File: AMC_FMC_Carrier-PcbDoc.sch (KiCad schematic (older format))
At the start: 17 parts

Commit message: Add two mounting holes
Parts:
- added B11, B12: PLATED_HOLE2.7_PAD5.0, Marble:HOLE2.7_PAD5.0, symbol Pads:PLATED_HOLE2.7_PAD5.0
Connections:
- wire segments 366 -> 368
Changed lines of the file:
@@
 	3400 15500 3600 15500
 Connection ~ 3400 15500
+$Comp
+L Pads:PLATED_HOLE2.7_PAD5.0 B11
+U 1 1 5ECD5570
+P 4000 15250
+F 0 "B11" H 3985 15355 50  0000 C CNN
+F 1 "PLATED_HOLE2.7_PAD5.0" H 4000 15080 60  0001 L CNN
+F 2 "Marble:HOLE2.7_PAD5.0" H 4000 14270 60  0001 L CNN
+F 3 "" H 4000 14900 60  0001 L CNN
+F 4 "Plated Hole" H 4000 14810 60  0001 L CNN "Pole4"
+F 5 "PLATED_HOLE2.7_PAD5.0" H 4000 14810 60  0001 L CNN "Part Number"
+F 6 "Single Terminal Socket" H 4000 14720 60  0001 L CNN "Library Ref"
+F 7 "SchLib\\Pads.SchLib" H 4000 14630 60  0001 L CNN "Library Path"
+F 8 " " H 4000 14540 60  0001 L CNN "Comment"
+F 9 "Standard (No BOM)" H 4000 14450 60  0001 L CNN "Component Kind"
+F 10 "Standard (No BOM)" H 4000 14360 60  0001 L CNN "Component Type"
+F 11 "1" H 4000 14180 60  0001 L CNN "Pin Count"
+F 12 " " H 4000 14090 60  0001 L CNN "Case"
+F 13 "PcbLib\\Pads.PcbLib" H 4000 14000 60  0001 L CNN "Footprint Path"
+F 14 "MTG270_500" H 4000 13910 60  0001 L CNN "Footprint Ref"
+F 15 "Plated Hole" H 4000 13820 60  0001 L CNN "Family"
+F 16 "No" H 4000 13730 60  0001 L CNN "Mounted"
+F 17 "No" H 4000 13640 60  0001 L CNN "Socket"
+F 18 "No" H 4000 13550 60  0001 L CNN "SMD"
+F 19 "No" H 4000 13460 60  0001 L CNN "Sense"
+F 20 " " H 4000 13370 60  0001 L CNN "Sense Comment"
+F 21 "None" H 4000 13280 60  0001 L CNN "Status"
+F 22 " " H 4000 13190 60  0001 L CNN "Status Comment"
+F 23 "Plated Through Hole: Hole Dia.=2.7mm Pad Dia.=5.0mm" H 4000 13010 60  0001 L CNN "Part Description"
+F 24 " " H 4000 12920 60  0001 L CNN "Manufacturer"
+F 25 " " H 4000 12830 60  0001 L CNN "Manufacturer Part Number"
+F 26 "0mm" H 4000 12740 60  0001 L CNN "ComponentHeight"
+F 27 " " H 4000 12650 60  0001 L CNN "Manufacturer1 Example"
+F 28 " " H 4000 12560 60  0001 L CNN "Manufacturer1 Part Number"
+F 29 " " H 4000 12470 60  0001 L CNN "Manufacturer1 ComponentHeight"
+F 30 " " H 4000 12200 60  0001 L CNN "ComponentLink1Description"
+F 31 " " H 4000 12020 60  0001 L CNN "ComponentLink2Description"
+F 32 "CERN DEM JMW" H 4000 11930 60  0001 L CNN "Author"
+F 33 "09/27/11 00:00:00" H 4000 11840 60  0001 L CNN "CreateDate"
+F 34 "09/27/11 00:00:00" H 4000 11750 60  0001 L CNN "LatestRevisionDate"
+F 35 "Plated Through Hole: Hole Dia.=2.7mm Pad Dia.=5.0mm" H 4000 11660 60  0001 L CNN "PackageDescription"
+F 36 "Eletro-mechanical.DbLib" H 4000 11570 60  0001 L CNN "Library Name"
+F 37 "This work is licensed under the Creative Commons CC-BY-SA 4.0 License. To the extent that circuit schematics that use Licensed Material can be considered to be ‘Adapted Material’, then the copyright holder waives article 3.b of the license with respect to these schematics." H 4000 11480 60  0001 L CNN "License"
+F 38 "dnf" H 4000 15250 50  0001 C CNN "config"
+	1    4000 15250
+	1    0    0    -1
+$EndComp
+$Comp
+L Pads:PLATED_HOLE2.7_PAD5.0 B12
+U 1 1 5ECD6329
+P 4150 15250
+F 0 "B12" H 4135 15355 50  0000 C CNN
+F 1 "PLATED_HOLE2.7_PAD5.0" H 4150 15080 60  0001 L CNN
+F 2 "Marble:HOLE2.7_PAD5.0" H 4150 14270 60  0001 L CNN
+F 3 "" H 4150 14900 60  0001 L CNN
+F 4 "Plated Hole" H 4150 14810 60  0001 L CNN "Pole4"
+F 5 "PLATED_HOLE2.7_PAD5.0" H 4150 14810 60  0001 L CNN "Part Number"
+F 6 "Single Terminal Socket" H 4150 14720 60  0001 L CNN "Library Ref"
+F 7 "SchLib\\Pads.SchLib" H 4150 14630 60  0001 L CNN "Library Path"
+F 8 " " H 4150 14540 60  0001 L CNN "Comment"
+F 9 "Standard (No BOM)" H 4150 14450 60  0001 L CNN "Component Kind"
+F 10 "Standard (No BOM)" H 4150 14360 60  0001 L CNN "Component Type"
+F 11 "1" H 4150 14180 60  0001 L CNN "Pin Count"
+F 12 " " H 4150 14090 60  0001 L CNN "Case"
+F 13 "PcbLib\\Pads.PcbLib" H 4150 14000 60  0001 L CNN "Footprint Path"
+F 14 "MTG270_500" H 4150 13910 60  0001 L CNN "Footprint Ref"
+F 15 "Plated Hole" H 4150 13820 60  0001 L CNN "Family"
+F 16 "No" H 4150 13730 60  0001 L CNN "Mounted"
+F 17 "No" H 4150 13640 60  0001 L CNN "Socket"
+F 18 "No" H 4150 13550 60  0001 L CNN "SMD"
+F 19 "No" H 4150 13460 60  0001 L CNN "Sense"
+F 20 " " H 4150 13370 60  0001 L CNN "Sense Comment"
+F 21 "None" H 4150 13280 60  0001 L CNN "Status"
+F 22 " " H 4150 13190 60  0001 L CNN "Status Comment"
+F 23 "Plated Through Hole: Hole Dia.=2.7mm Pad Dia.=5.0mm" H 4150 13010 60  0001 L CNN "Part Description"
+F 24 " " H 4150 12920 60  0001 L CNN "Manufacturer"
+F 25 " " H 4150 12830 60  0001 L CNN "Manufacturer Part Number"
+F 26 "0mm" H 4150 12740 60  0001 L CNN "ComponentHeight"
+F 27 " " H 4150 12650 60  0001 L CNN "Manufacturer1 Example"
+F 28 " " H 4150 12560 60  0001 L CNN "Manufacturer1 Part Number"
+F 29 " " H 4150 12470 60  0001 L CNN "Manufacturer1 ComponentHeight"
+F 30 " " H 4150 12200 60  0001 L CNN "ComponentLink1Description"
+F 31 " " H 4150 12020 60  0001 L CNN "ComponentLink2Description"
+F 32 "CERN DEM JMW" H 4150 11930 60  0001 L CNN "Author"
+F 33 "09/27/11 00:00:00" H 4150 11840 60  0001 L CNN "CreateDate"
+F 34 "09/27/11 00:00:00" H 4150 11750 60  0001 L CNN "LatestRevisionDate"
+F 35 "Plated Through Hole: Hole Dia.=2.7mm Pad Dia.=5.0mm" H 4150 11660 60  0001 L CNN "PackageDescription"
+F 36 "Eletro-mechanical.DbLib" H 4150 11570 60  0001 L CNN "Library Name"
+F 37 "This work is licensed under the Creative Commons CC-BY-SA 4.0 License. To the extent that circuit schematics that use Licensed Material can be considered to be ‘Adapted Material’, then the copyright holder waives article 3.b of the license with respect to these schematics." H 4150 11480 60  0001 L CNN "License"
+F 38 "dnf" H 4150 15250 50  0001 C CNN "config"
+	1    4150 15250
+	1    0    0    -1
+$EndComp
+$Comp
+L power:GND #PWR?
+U 1 1 5ECDA445
+P 4350 15250
+AR Path="/5BD32060/5ECDA445" Ref="#PWR?"  Part="1"
+AR Path="/5BABAC65/5ECDA445" Ref="#PWR?"  Part="1"
+AR Path="/5CC24E97/5ECDA445" Ref="#PWR?"  Part="1"
+AR Path="/5CC393D3/5ECDA445" Ref="#PWR?"  Part="1"
+AR Path="/5CC6DBF7/5ECDA445" Ref="#PWR?"  Part="1"
+AR Path="/5CC8AFE1/5ECDA445" Ref="#PWR?"  Part="1"
+AR Path="/5BCEDA3D/5ECDA445" Ref="#PWR?"  Part="1"
+AR Path="/5ECDA445" Ref="#PWR?"  Part="1"
+F 0 "#PWR?" H 4350 15000 50  0001 C CNN
+F 1 "GND" H 4355 15077 50  0000 C CNN
+F 2 "" H 4350 15250 50  0001 C CNN
+F 3 "" H 4350 15250 50  0001 C CNN
+	1    4350 15250
+	1    0    0    -1
+$EndComp
+Wire Wire Line
+	4000 15250 4150 15250
+Wire Wire Line
+	4150 15250 4350 15250
+Connection ~ 4150 15250
 $EndSCHEMATC

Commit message: More attribute fixes
Fix up Attribute names in HDT0001 and AG5300
Remove stray attribute for SN65MLVD2DRBT (added in last commit)
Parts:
- S1: Manufacturer (none) -> C & K COMPONENTS; Manufacturer_Name C & K COMPONENTS -> (none)
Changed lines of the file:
@@
 F 4 "HDT0001 (Detector Switches)" H 4000 9100 50  0001 L CNN "Description"
 F 5 "3" H 4000 9000 50  0001 L CNN "Height"
-F 6 "C & K COMPONENTS" H 4000 8900 50  0001 L CNN "Manufacturer_Name"
+F 6 "C & K COMPONENTS" H 4000 8900 50  0001 L CNN "Manufacturer"
 F 7 "HDT0001" H 4000 8800 50  0001 L CNN "Manufacturer Part Number"
 F 8 "7931598" H 4000 8700 50  0001 L CNN "RS Part Number"

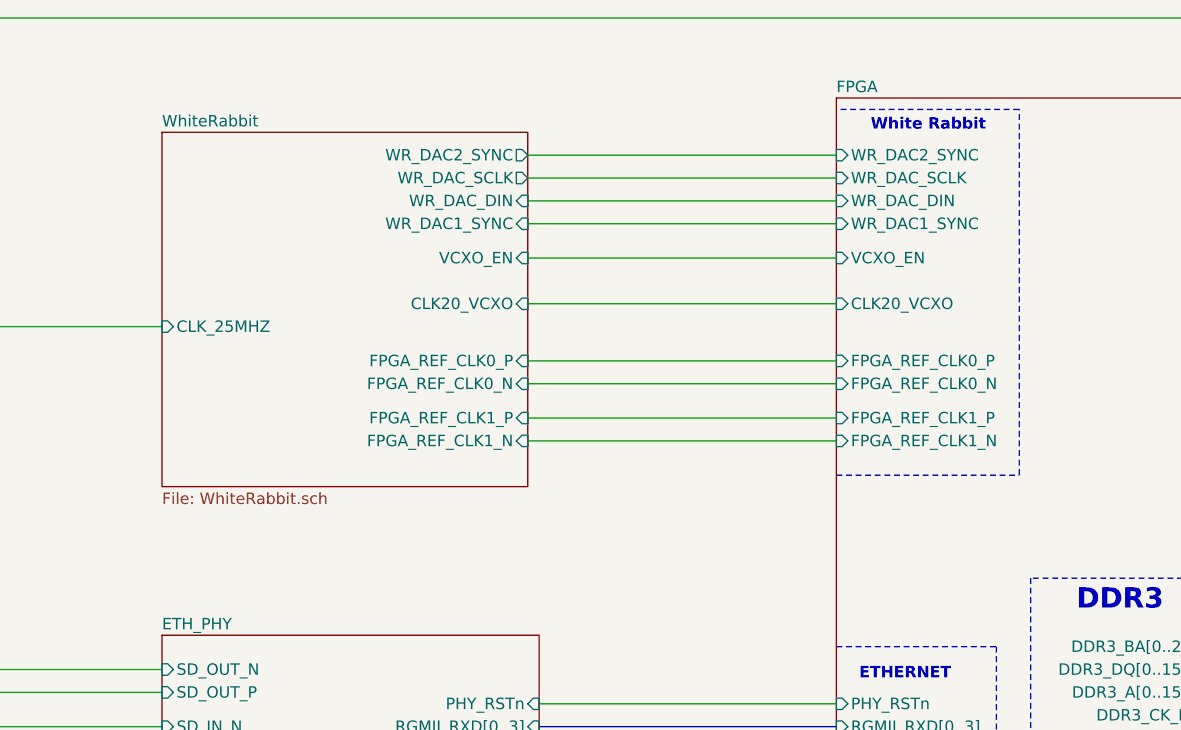
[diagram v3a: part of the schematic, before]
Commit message: added SI570, U39 3V3 -> 3V3P
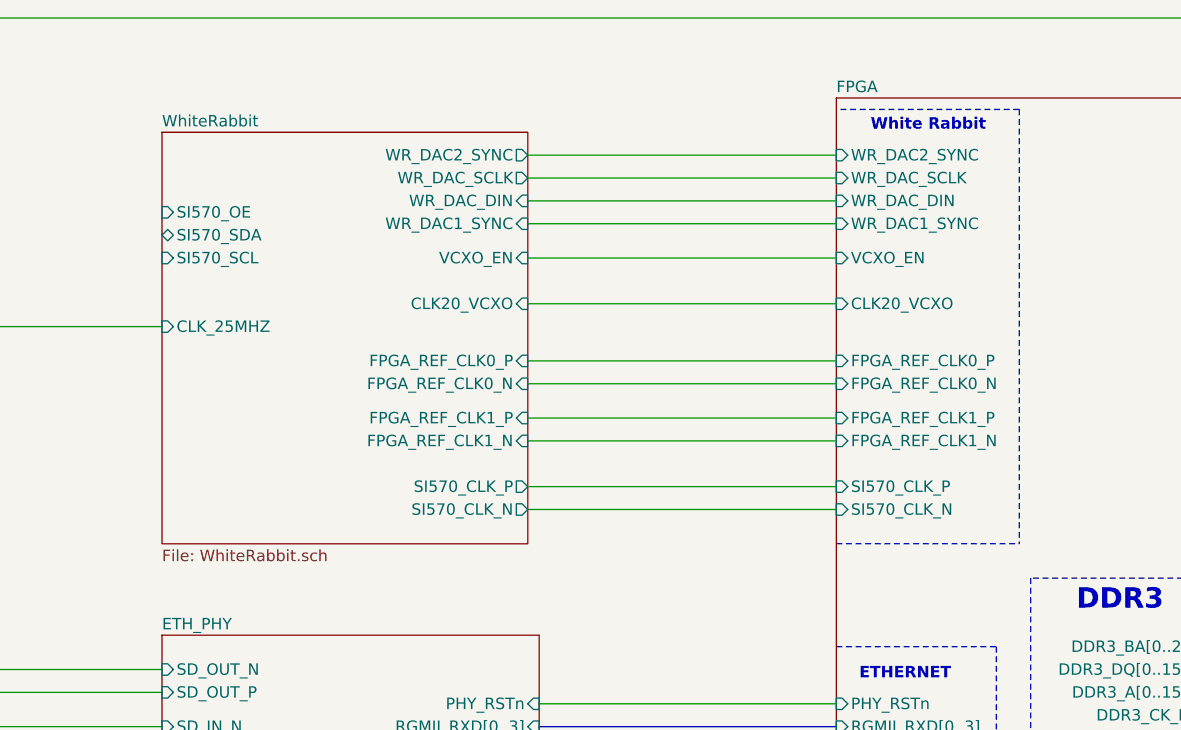
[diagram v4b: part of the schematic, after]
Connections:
- wire segments 368 -> 370
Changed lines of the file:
@@
 SFP4
 $Sheet
-S 8400 1700 1600 1550
+S 8400 1700 1600 1800
 U 5C16BF13
 F0 "WhiteRabbit" 50
@@
 F11 "FPGA_REF_CLK1_N" I R 10000 3050 50
 F12 "CLK_25MHZ" I L 8400 2550 50
+F13 "SI570_CLK_P" O R 10000 3250 50
+F14 "SI570_CLK_N" O R 10000 3350 50
+F15 "SI570_OE" I L 8400 2050 50
+F16 "SI570_SDA" B L 8400 2150 50
+F17 "SI570_SCL" I L 8400 2250 50
 $EndSheet
 $Sheet
@@
 F126 "RGMII_RX_DV" I L 11350 4700 50
 F127 "RGMII_RX_CLK" I L 11350 4800 50
+F128 "SI570_CLK_P" I L 11350 3250 50
+F129 "SI570_CLK_N" I L 11350 3350 50
 $EndSheet
 Wire Wire Line
@@
 Wire Bus Line
 	12950 7750 14200 7750
-Wire Notes Line
-	11350 3200 12150 3200
-Wire Notes Line
-	12150 3200 12150 1600
 Wire Notes Line
 	12150 1600 11350 1600
@@
 	4150 15250 4350 15250
 Connection ~ 4150 15250
+Wire Notes Line
+	11350 3500 12150 3500
+Wire Notes Line
+	12150 1600 12150 3500
+Wire Wire Line
+	10000 3250 11350 3250
+Wire Wire Line
+	10000 3350 11350 3350
 $EndSCHEMATC

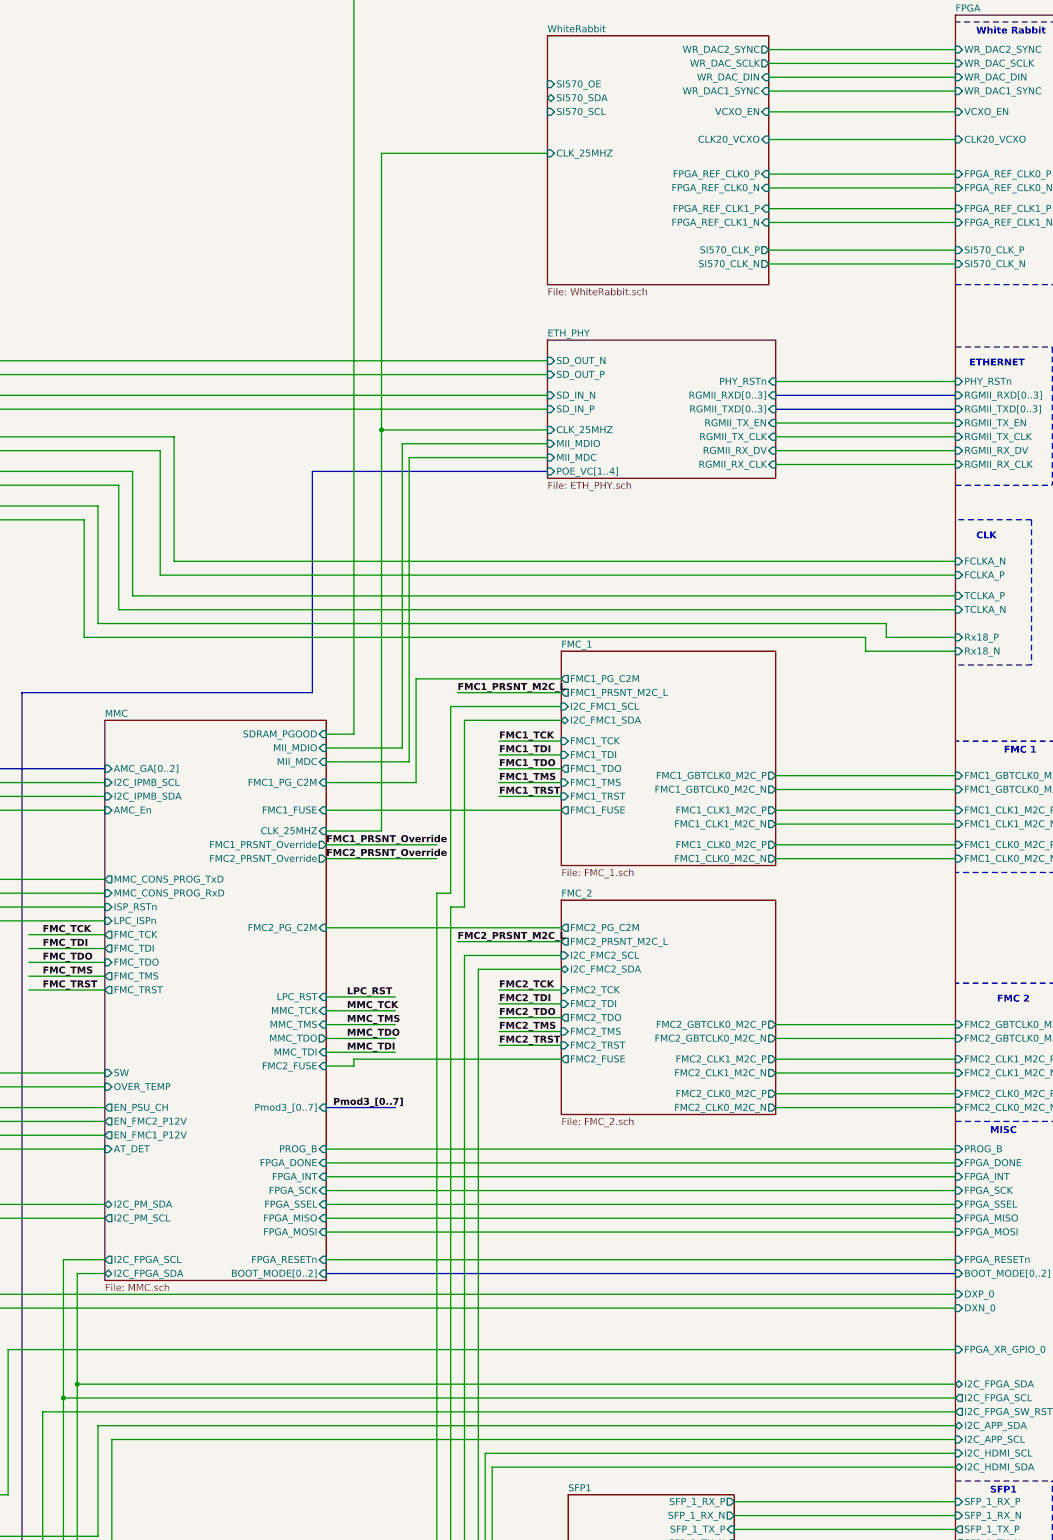
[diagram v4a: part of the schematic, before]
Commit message: More work on Si570 circuit
Attach SI570_{SCL,SDA} to I2C_APP
Make a part number for Y6 visible on schematic
Mark Y6 Si570 as dnf
Mark C385 C386 as dnf
Layout passes DRC
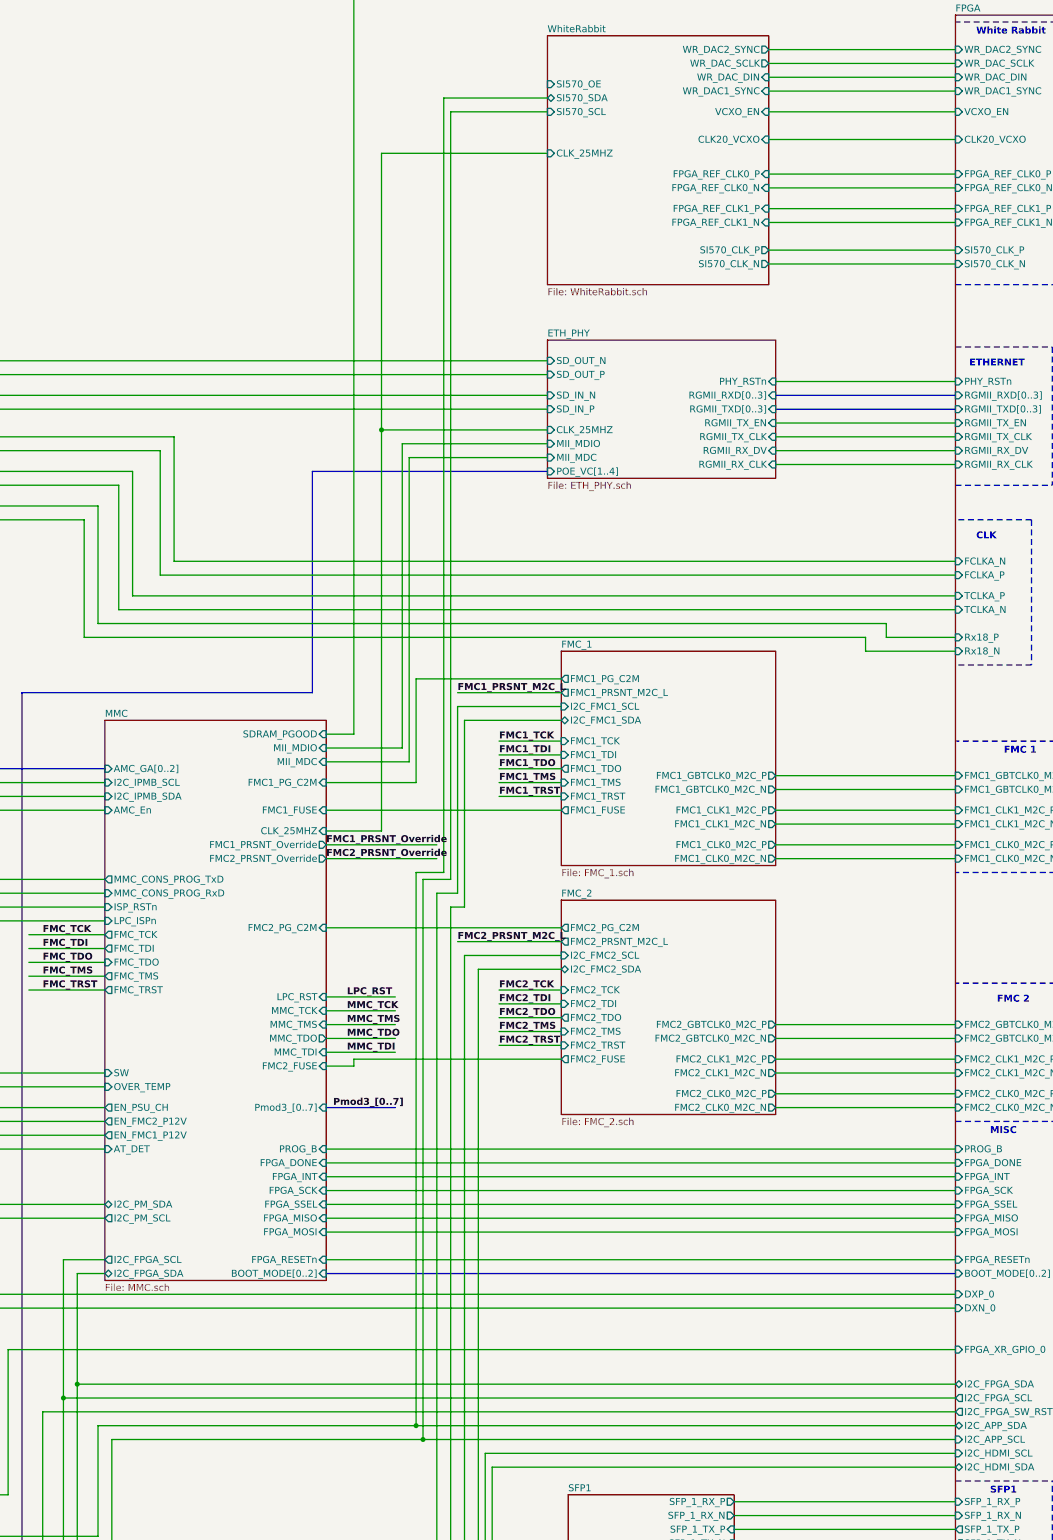
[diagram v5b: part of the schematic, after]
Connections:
- wire segments 370 -> 380
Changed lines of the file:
@@
 	4250 12650 3900 12650
 Wire Wire Line
-	11350 11750 5150 11750
+	11350 11750 7450 11750
 Wire Wire Line
 	5150 11750 5150 12550
@@
 Connection ~ 4350 12550
 Wire Wire Line
-	11350 11850 5250 11850
+	11350 11850 7500 11850
 Wire Wire Line
 	5250 11850 5250 12650
@@
 	7800 6650 8500 6650
 Wire Wire Line
-	7600 7900 7700 7900
-Wire Wire Line
-	7700 7900 7700 6550
-Wire Wire Line
 	7600 7900 7600 13000
-Wire Wire Line
-	7700 6550 8500 6550
 Wire Wire Line
 	7600 7550 6800 7550
@@
 Wire Wire Line
 	10000 3350 11350 3350
+Wire Wire Line
+	8400 2250 7700 2250
+Wire Wire Line
+	7500 7800 7500 11850
+Connection ~ 7500 11850
+Wire Wire Line
+	7500 11850 5250 11850
+Wire Wire Line
+	8400 2150 7650 2150
+Wire Wire Line
+	7450 7750 7450 11750
+Connection ~ 7450 11750
+Wire Wire Line
+	7450 11750 5150 11750
+Wire Wire Line
+	7750 7900 7750 6550
+Wire Wire Line
+	7750 6550 8500 6550
+Wire Wire Line
+	7600 7900 7750 7900
+Wire Wire Line
+	7700 7800 7700 2250
+Wire Wire Line
+	7500 7800 7700 7800
+Wire Wire Line
+	7650 2150 7650 7750
+Wire Wire Line
+	7450 7750 7650 7750
 $EndSCHEMATC
